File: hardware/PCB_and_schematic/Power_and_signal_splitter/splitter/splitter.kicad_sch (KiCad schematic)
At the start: 14 parts, among them J1 SIGNAL_TERMINAL, J2 DC_POWER_SUPPLY, J3 DIODE_PROBE, J4 OPTICAL_PROBE, J5 DC_POWER_SUPPLY, J6 DC_POWER_SUPPLY, J7 UNUSED, U1 L7812

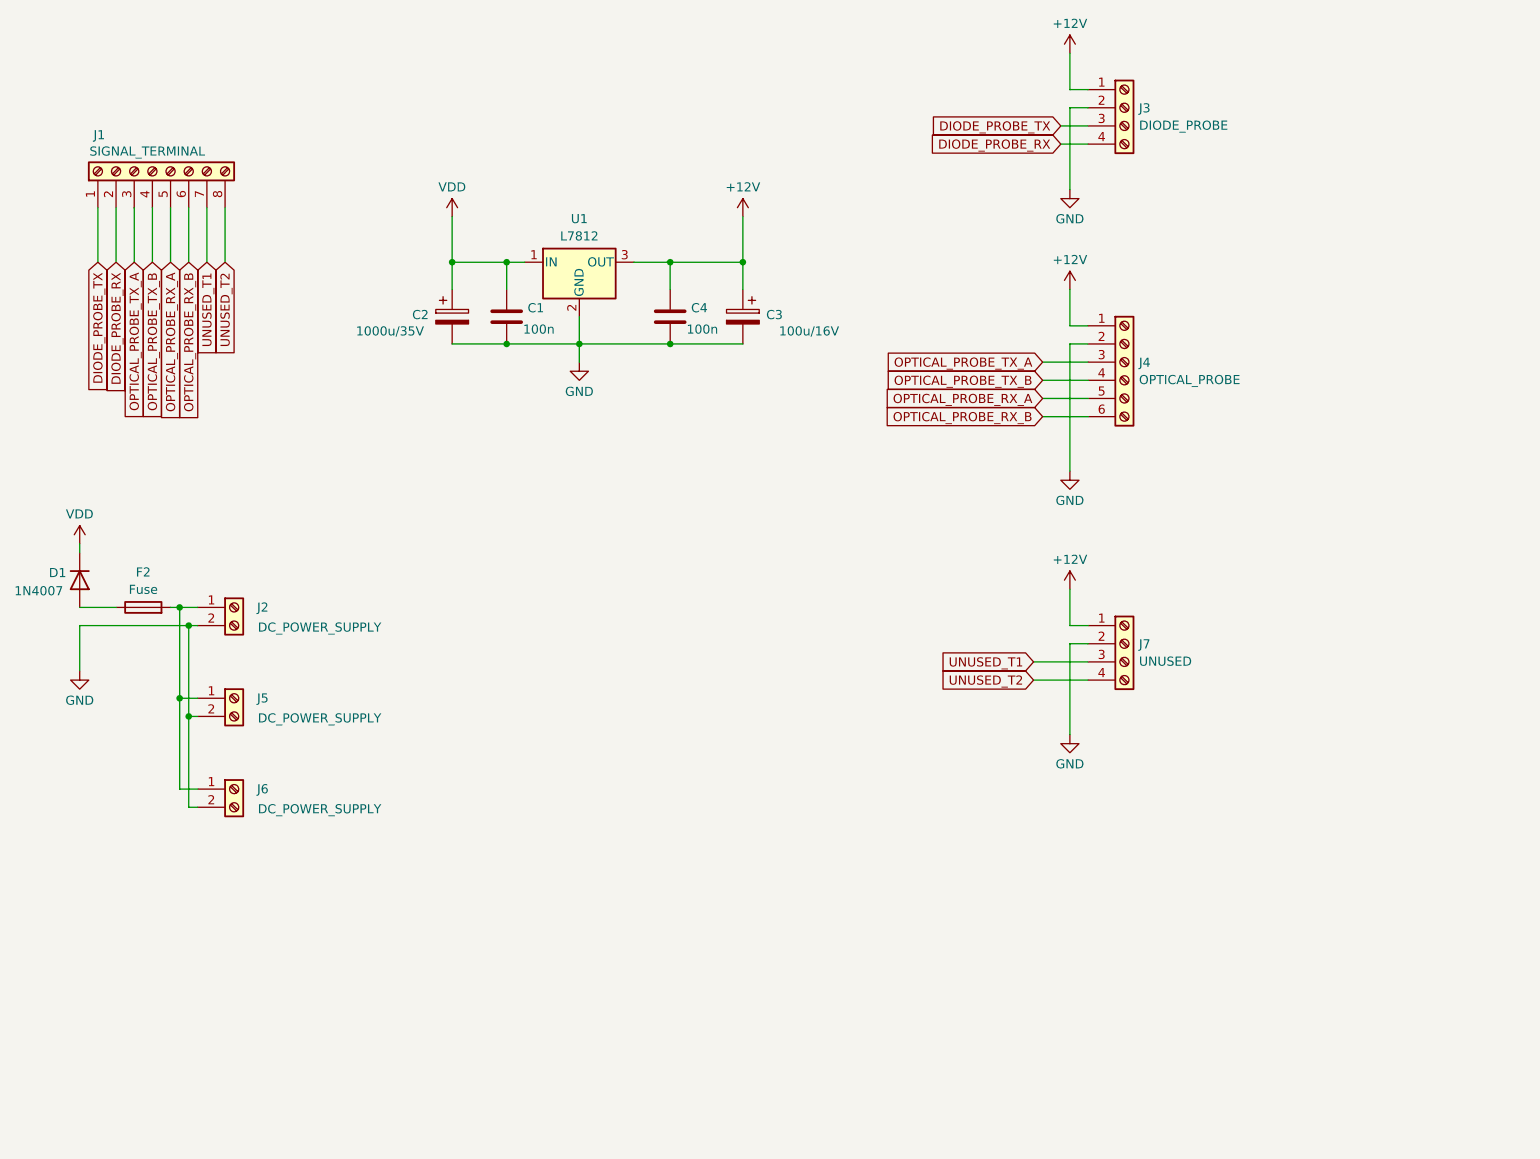
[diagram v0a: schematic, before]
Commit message: Splitter PCB, connectors esp board
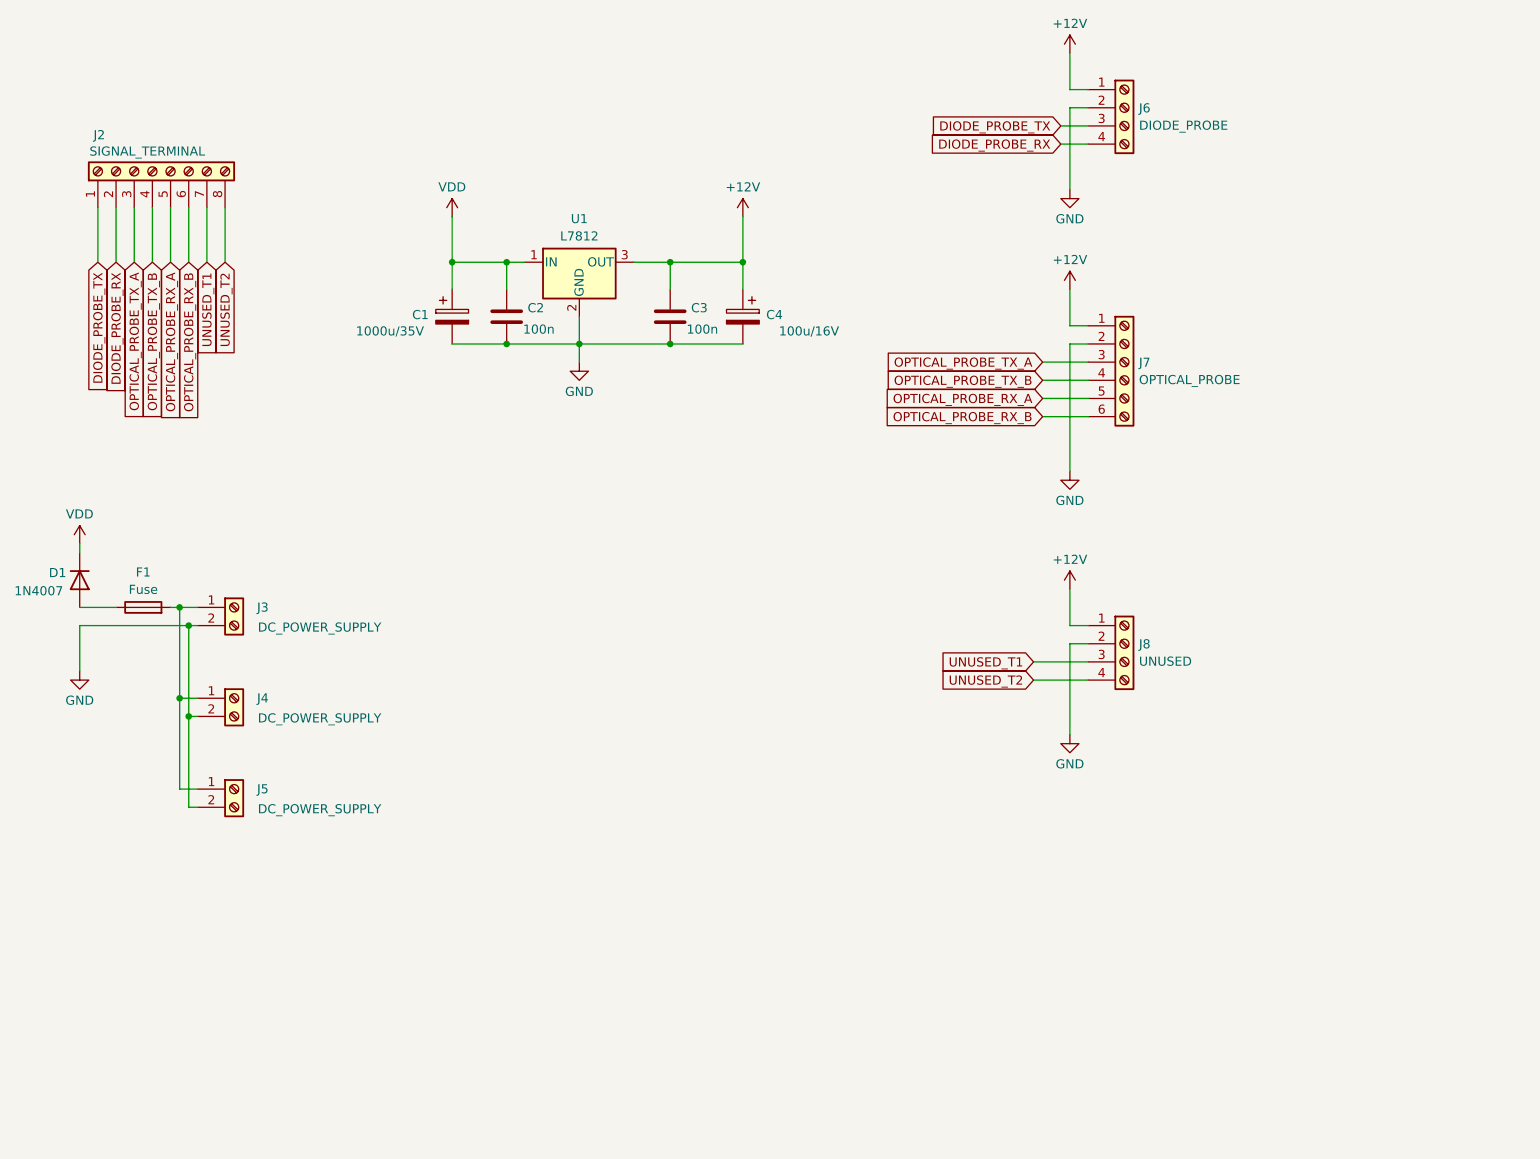
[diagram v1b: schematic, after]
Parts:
- C1: renamed from C2; footprint (none) -> Capacitor_THT:CP_Radial_D10.0mm_P3.80mm
- C2: renamed from C1; footprint (none) -> Capacitor_SMD:C_0805_2012Metric
- C3: renamed from C4; footprint (none) -> Capacitor_SMD:C_0805_2012Metric
- C4: renamed from C3; footprint (none) -> Capacitor_THT:CP_Radial_D8.0mm_P3.50mm
- F1: renamed from F2; footprint (none) -> Fuse:Fuseholder_Clip-5x20mm_Eaton_1A5601-01_Inline_P20.80x6.76mm_D1.70mm_Horizontal
- J2: renamed from J1; footprint (none) -> TerminalBlock:TerminalBlock_bornier-8_P5.08mm
- J3: renamed from J2; footprint (none) -> TerminalBlock:TerminalBlock_Altech_AK300-2_P5.00mm
- J4: renamed from J5; footprint (none) -> TerminalBlock:TerminalBlock_Altech_AK300-2_P5.00mm
- J5: renamed from J6; footprint (none) -> TerminalBlock:TerminalBlock_Altech_AK300-2_P5.00mm
- J6: renamed from J3; footprint (none) -> TerminalBlock:TerminalBlock_Altech_AK300-4_P5.00mm
- J7: renamed from J4; footprint (none) -> TerminalBlock:TerminalBlock_bornier-6_P5.08mm
- J8: renamed from J7; footprint (none) -> TerminalBlock:TerminalBlock_Altech_AK300-4_P5.00mm
- U1: footprint (none) -> Package_TO_SOT_THT:TO-220-3_Vertical
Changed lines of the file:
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@@
 		(on_board yes)
 		(dnp no)
-		(property "Reference" "C2"
+		(property "Reference" "C1"
 			(at 70.612 60.706 0)
 			(effects
@@
 			)
 		)
-		(property "Footprint" ""
+		(property "Footprint" "Capacitor_THT:CP_Radial_D10.0mm_P3.80mm"
 			(at 77.1652 64.77 0)
 			(effects
@@
 			(project "splitter"
 				(path "/0286cab7-ab30-426b-8345-1f03e11d2c7c"
-					(reference "C2")
+					(reference "C1")
 					(unit 1)
 				)
@@
 		(dnp no)
 		(fields_autoplaced yes)
-		(property "Reference" "#PWR05"
+		(property "Reference" "#PWR04"
 			(at 93.98 73.66 0)
 			(effects
@@
 			(project "splitter"
 				(path "/0286cab7-ab30-426b-8345-1f03e11d2c7c"
-					(reference "#PWR05")
+					(reference "#PWR04")
 					(unit 1)
 				)
@@
 		(dnp no)
 		(fields_autoplaced yes)
-		(property "Reference" "#PWR04"
+		(property "Reference" "#PWR05"
 			(at 116.84 50.8 0)
 			(effects
@@
 			(project "splitter"
 				(path "/0286cab7-ab30-426b-8345-1f03e11d2c7c"
-					(reference "#PWR04")
+					(reference "#PWR05")
 					(unit 1)
 				)
@@
 		(dnp no)
 		(fields_autoplaced yes)
-		(property "Reference" "#PWR09"
+		(property "Reference" "#PWR07"
 			(at 162.56 49.53 0)
 			(effects
@@
 			(project "splitter"
 				(path "/0286cab7-ab30-426b-8345-1f03e11d2c7c"
-					(reference "#PWR09")
+					(reference "#PWR07")
 					(unit 1)
 				)
@@
 		(on_board yes)
 		(dnp no)
-		(property "Reference" "C3"
+		(property "Reference" "C4"
 			(at 122.428 60.706 0)
 			(effects
@@
 			)
 		)
-		(property "Footprint" ""
+		(property "Footprint" "Capacitor_THT:CP_Radial_D8.0mm_P3.50mm"
 			(at 115.8748 64.77 0)
 			(effects
@@
 			(project "splitter"
 				(path "/0286cab7-ab30-426b-8345-1f03e11d2c7c"
-					(reference "C3")
+					(reference "C4")
 					(unit 1)
 				)
@@
 		(dnp no)
 		(fields_autoplaced yes)
-		(property "Reference" "#PWR01"
+		(property "Reference" "#PWR02"
 			(at 24.13 116.84 0)
 			(effects
@@
 			(project "splitter"
 				(path "/0286cab7-ab30-426b-8345-1f03e11d2c7c"
-					(reference "#PWR01")
+					(reference "#PWR02")
 					(unit 1)
 				)
@@
 		(dnp no)
 		(fields_autoplaced yes)
-		(property "Reference" "#PWR08"
+		(property "Reference" "#PWR09"
 			(at 162.56 88.9 0)
 			(effects
@@
 			(project "splitter"
 				(path "/0286cab7-ab30-426b-8345-1f03e11d2c7c"
-					(reference "#PWR08")
+					(reference "#PWR09")
 					(unit 1)
 				)
@@
 			)
 		)
-		(property "Footprint" ""
+		(property "Footprint" "Package_TO_SOT_THT:TO-220-3_Vertical"
 			(at 94.615 57.15 0)
 			(effects
@@
 		(dnp no)
 		(fields_autoplaced yes)
-		(property "Reference" "J4"
+		(property "Reference" "J7"
 			(at 172.212 67.3678 0)
 			(effects
@@
 			)
 		)
-		(property "Footprint" ""
+		(property "Footprint" "TerminalBlock:TerminalBlock_bornier-6_P5.08mm"
 			(at 170.18 67.31 0)
 			(effects
@@
 			(project "splitter"
 				(path "/0286cab7-ab30-426b-8345-1f03e11d2c7c"
-					(reference "J4")
+					(reference "J7")
 					(unit 1)
 				)
@@
 		(dnp no)
 		(fields_autoplaced yes)
-		(property "Reference" "#PWR02"
+		(property "Reference" "#PWR01"
 			(at 24.13 96.52 0)
 			(effects
@@
 			(project "splitter"
 				(path "/0286cab7-ab30-426b-8345-1f03e11d2c7c"
-					(reference "#PWR02")
+					(reference "#PWR01")
 					(unit 1)
 				)
@@
 		(dnp no)
 		(fields_autoplaced yes)
-		(property "Reference" "F2"
+		(property "Reference" "F1"
 			(at 33.02 96.6935 90)
 			(effects
@@
 			)
 		)
-		(property "Footprint" ""
+		(property "Footprint" "Fuse:Fuseholder_Clip-5x20mm_Eaton_1A5601-01_Inline_P20.80x6.76mm_D1.70mm_Horizontal"
 			(at 33.02 103.378 90)
 			(effects
@@
 			(project "splitter"
 				(path "/0286cab7-ab30-426b-8345-1f03e11d2c7c"
-					(reference "F2")
+					(reference "F1")
 					(unit 1)
 				)
@@
 		(on_board yes)
 		(dnp no)
-		(property "Reference" "J5"
+		(property "Reference" "J4"
 			(at 50.546 114.3 0)
 			(effects
@@
 			)
 		)
-		(property "Footprint" ""
+		(property "Footprint" "TerminalBlock:TerminalBlock_Altech_AK300-2_P5.00mm"
 			(at 45.72 114.3 0)
 			(effects
@@
 			(project "splitter"
 				(path "/0286cab7-ab30-426b-8345-1f03e11d2c7c"
-					(reference "J5")
+					(reference "J4")
 					(unit 1)
 				)
@@
 		(on_board yes)
 		(dnp no)
-		(property "Reference" "C4"
+		(property "Reference" "C3"
 			(at 109.601 59.7478 0)
 			(effects
@@
 			)
 		)
-		(property "Footprint" ""
+		(property "Footprint" "Capacitor_SMD:C_0805_2012Metric"
 			(at 107.6452 64.77 0)
 			(effects
@@
 			(project "splitter"
 				(path "/0286cab7-ab30-426b-8345-1f03e11d2c7c"
-					(reference "C4")
+					(reference "C3")
 					(unit 1)
 				)
@@
 		(on_board yes)
 		(dnp no)
-		(property "Reference" "J2"
+		(property "Reference" "J3"
 			(at 50.546 101.6 0)
 			(effects
@@
 			)
 		)
-		(property "Footprint" ""
+		(property "Footprint" "TerminalBlock:TerminalBlock_Altech_AK300-2_P5.00mm"
 			(at 45.72 101.6 0)
 			(effects
@@
 			(project "splitter"
 				(path "/0286cab7-ab30-426b-8345-1f03e11d2c7c"
-					(reference "J2")
+					(reference "J3")
 					(unit 1)
 				)
@@
 		(on_board yes)
 		(dnp no)
-		(property "Reference" "J6"
+		(property "Reference" "J5"
 			(at 50.546 127 0)
 			(effects
@@
 			)
 		)
-		(property "Footprint" ""
+		(property "Footprint" "TerminalBlock:TerminalBlock_Altech_AK300-2_P5.00mm"
 			(at 45.72 127 0)
 			(effects
@@
 			(project "splitter"
 				(path "/0286cab7-ab30-426b-8345-1f03e11d2c7c"
-					(reference "J6")
+					(reference "J5")
 					(unit 1)
 				)
@@
 		(dnp no)
 		(fields_autoplaced yes)
-		(property "Reference" "J7"
+		(property "Reference" "J8"
 			(at 172.212 106.7378 0)
 			(effects
@@
 			)
 		)
-		(property "Footprint" ""
+		(property "Footprint" "TerminalBlock:TerminalBlock_Altech_AK300-4_P5.00mm"
 			(at 170.18 106.68 0)
 			(effects
@@
 			(project "splitter"
 				(path "/0286cab7-ab30-426b-8345-1f03e11d2c7c"
-					(reference "J7")
+					(reference "J8")
 					(unit 1)
 				)
@@
 		(on_board yes)
 		(dnp no)
-		(property "Reference" "J1"
+		(property "Reference" "J2"
 			(at 27.686 35.56 90)
 			(effects
@@
 			)
 		)
-		(property "Footprint" ""
+		(property "Footprint" "TerminalBlock:TerminalBlock_bornier-8_P5.08mm"
 			(at 34.29 40.64 0)
 			(effects
@@
 			(project "splitter"
 				(path "/0286cab7-ab30-426b-8345-1f03e11d2c7c"
-					(reference "J1")
+					(reference "J2")
 					(unit 1)
 				)
@@
 		(dnp no)
 		(fields_autoplaced yes)
-		(property "Reference" "#PWR07"
+		(property "Reference" "#PWR08"
 			(at 162.56 60.96 0)
 			(effects
@@
 			(project "splitter"
 				(path "/0286cab7-ab30-426b-8345-1f03e11d2c7c"
-					(reference "#PWR07")
+					(reference "#PWR08")
 					(unit 1)
 				)
@@
 		(dnp no)
 		(fields_autoplaced yes)
-		(property "Reference" "J3"
+		(property "Reference" "J6"
 			(at 172.212 31.8078 0)
 			(effects
@@
 			)
 		)
-		(property "Footprint" ""
+		(property "Footprint" "TerminalBlock:TerminalBlock_Altech_AK300-4_P5.00mm"
 			(at 170.18 31.75 0)
 			(effects
@@
 			(project "splitter"
 				(path "/0286cab7-ab30-426b-8345-1f03e11d2c7c"
-					(reference "J3")
+					(reference "J6")
 					(unit 1)
 				)
@@
 		(on_board yes)
 		(dnp no)
-		(property "Reference" "C1"
+		(property "Reference" "C2"
 			(at 86.741 59.7478 0)
 			(effects
@@
 			)
 		)
-		(property "Footprint" ""
+		(property "Footprint" "Capacitor_SMD:C_0805_2012Metric"
 			(at 84.7852 64.77 0)
 			(effects
@@
 			(project "splitter"
 				(path "/0286cab7-ab30-426b-8345-1f03e11d2c7c"
-					(reference "C1")
-					(unit 1)
-				)
+					(reference "C2")
+					(unit 1)
+				)

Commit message: Splitters
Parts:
- removed C1: 1000u/35V, Capacitor_THT:CP_Radial_D10.0mm_P3.80mm, symbol Device:C_Polarized
- removed C2, C3: 100n, Capacitor_SMD:C_0805_2012Metric, symbol Device:C
- removed C4: 100u/16V, Capacitor_THT:CP_Radial_D8.0mm_P3.50mm, symbol Device:C_Polarized
- removed D1: 1N4007, Diode_THT:D_DO-41_SOD81_P10.16mm_Horizontal, symbol Diode:1N4007
- removed F1: Fuse, Fuse:Fuseholder_Clip-5x20mm_Eaton_1A5601-01_Inline_P20.80x6.76mm_D1.70mm_Horizontal, symbol Device:Fuse
- removed J2: SIGNAL_TERMINAL, TerminalBlock:TerminalBlock_bornier-8_P5.08mm, symbol Connector:Screw_Terminal_01x08
- removed J3, J4, J5: DC_POWER_SUPPLY, TerminalBlock:TerminalBlock_Altech_AK300-2_P5.00mm, symbol Connector:Screw_Terminal_01x02
- removed J6: DIODE_PROBE, TerminalBlock:TerminalBlock_Altech_AK300-4_P5.00mm, symbol Connector:Screw_Terminal_01x04
- removed J7: OPTICAL_PROBE, TerminalBlock:TerminalBlock_bornier-6_P5.08mm, symbol Connector:Screw_Terminal_01x06
- removed J8: UNUSED, TerminalBlock:TerminalBlock_Altech_AK300-4_P5.00mm, symbol Connector:Screw_Terminal_01x04
- removed U1: L7812, Package_TO_SOT_THT:TO-220-3_Vertical, symbol Regulator_Linear:L7812
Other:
- added sheet Probe Splitter (probe_splitter.kicad_sch)
- added sheet Router and Camera Power Supply (router_camera_power_supply.kicad_sch)
